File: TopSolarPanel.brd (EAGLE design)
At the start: 81 x 81 mm, 19 parts

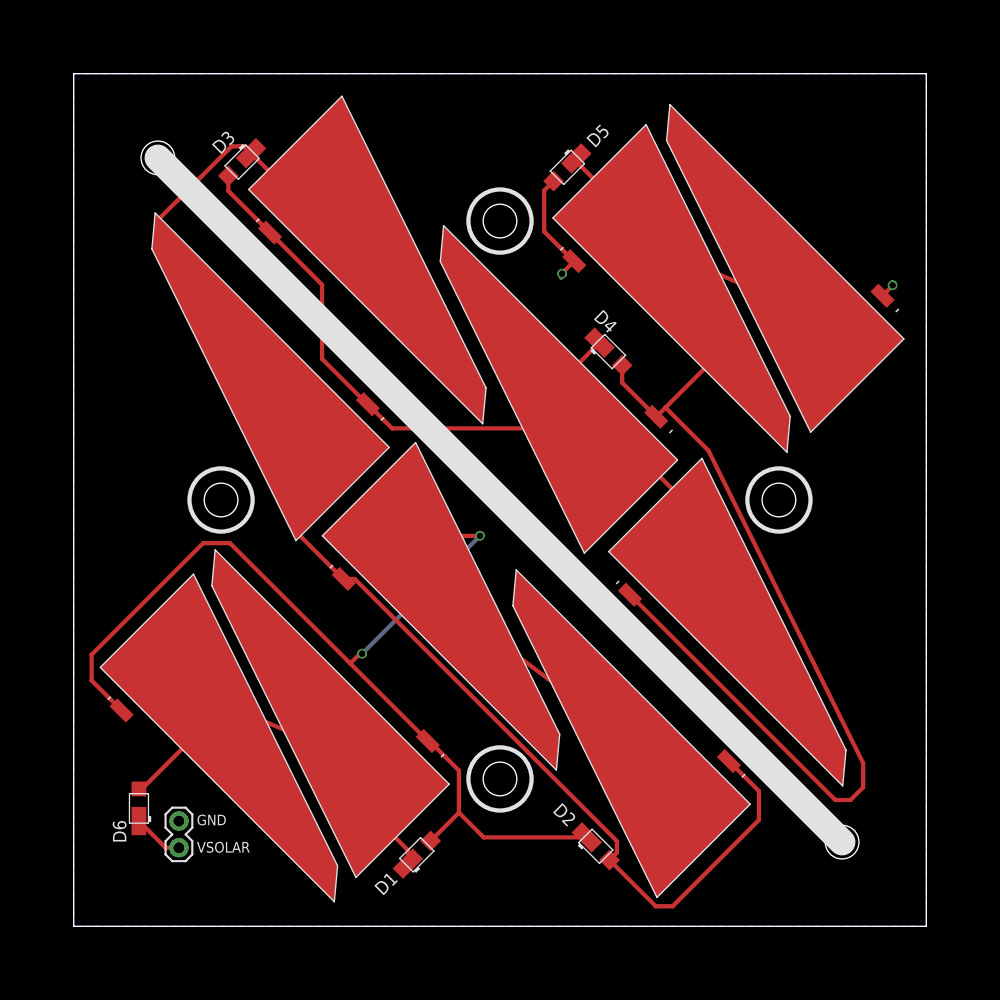
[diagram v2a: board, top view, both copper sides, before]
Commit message: Changed top board dimensions
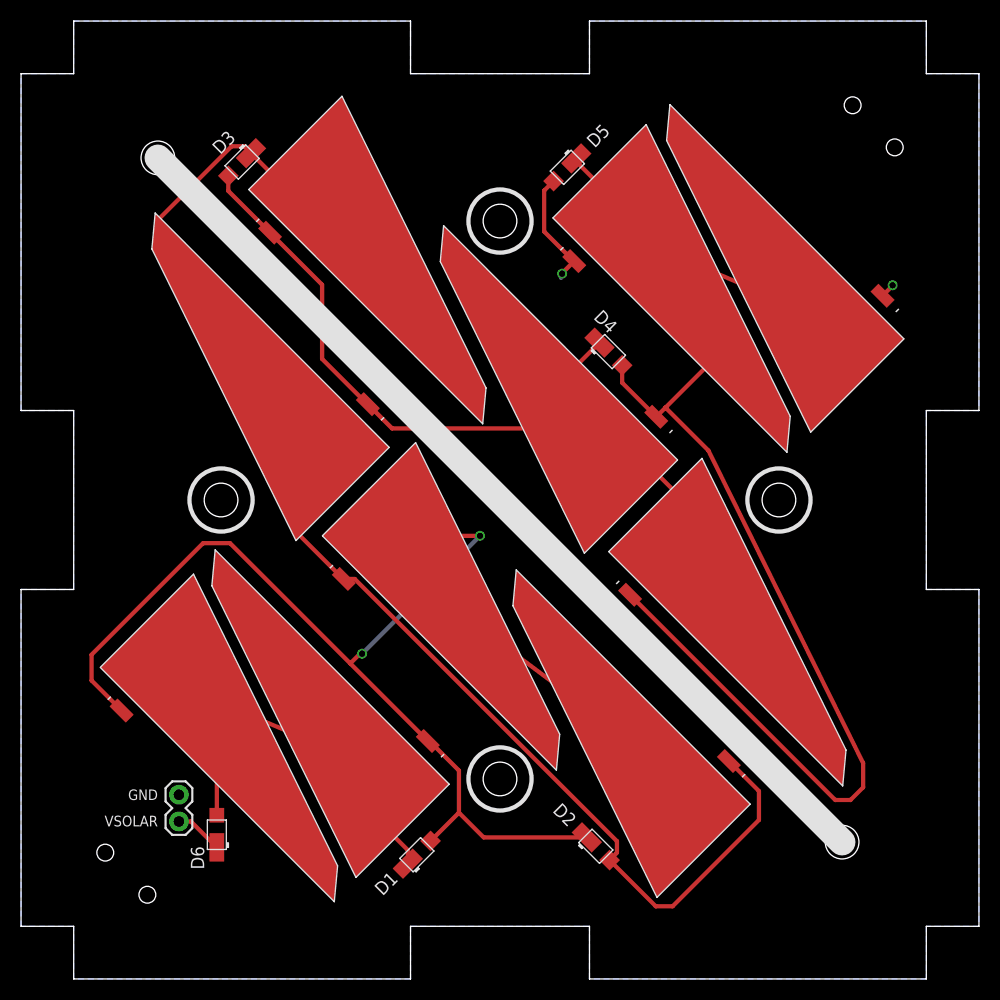
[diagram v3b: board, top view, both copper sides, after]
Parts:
- moved D6 7.81 mm to (13.6, 8.70)
- moved JP5 2.50 mm to (10.0, 12.5)
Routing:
- net N$9: track 57.5 -> 56.7 mm
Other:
- board size 81 x 81 mm -> 91 x 91 mm
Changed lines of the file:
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@@
 <board>
 <plain>
-<wire x1="0" y1="81" x2="0" y2="0" width="0" layer="20"/>
-<wire x1="0" y1="0" x2="81" y2="0" width="0" layer="20"/>
-<wire x1="81" y1="0" x2="81" y2="81" width="0" layer="20"/>
-<wire x1="81" y1="81" x2="0" y2="81" width="0" layer="20"/>
+<wire x1="0" y1="86" x2="0" y2="81" width="0" layer="20"/>
+<wire x1="0" y1="81" x2="-5" y2="81" width="0" layer="20"/>
+<wire x1="-5" y1="81" x2="-5" y2="49" width="0" layer="20"/>
+<wire x1="-5" y1="49" x2="0" y2="49" width="0" layer="20"/>
+<wire x1="0" y1="49" x2="0" y2="32" width="0" layer="20"/>
+<wire x1="0" y1="32" x2="-5" y2="32" width="0" layer="20"/>
+<wire x1="-5" y1="32" x2="-5" y2="0" width="0" layer="20"/>
+<wire x1="-5" y1="0" x2="0" y2="0" width="0" layer="20"/>
+<wire x1="0" y1="0" x2="0" y2="-5" width="0" layer="20"/>
+<wire x1="0" y1="-5" x2="32" y2="-5" width="0" layer="20"/>
+<wire x1="32" y1="-5" x2="32" y2="0" width="0" layer="20"/>
+<wire x1="32" y1="0" x2="49" y2="0" width="0" layer="20"/>
+<wire x1="49" y1="0" x2="49" y2="-5" width="0" layer="20"/>
+<wire x1="49" y1="-5" x2="81" y2="-5" width="0" layer="20"/>
+<wire x1="81" y1="-5" x2="81" y2="0" width="0" layer="20"/>
+<wire x1="81" y1="0" x2="86" y2="0" width="0" layer="20"/>
+<wire x1="86" y1="0" x2="86" y2="32" width="0" layer="20"/>
+<wire x1="86" y1="32" x2="81" y2="32" width="0" layer="20"/>
+<wire x1="81" y1="32" x2="81" y2="49" width="0" layer="20"/>
+<wire x1="81" y1="49" x2="86" y2="49" width="0" layer="20"/>
+<wire x1="86" y1="49" x2="86" y2="81" width="0" layer="20"/>
+<wire x1="86" y1="81" x2="81" y2="81" width="0" layer="20"/>
+<wire x1="81" y1="81" x2="81" y2="86" width="0" layer="20"/>
+<wire x1="81" y1="86" x2="49" y2="86" width="0" layer="20"/>
+<wire x1="49" y1="86" x2="49" y2="81" width="0" layer="20"/>
+<wire x1="49" y1="81" x2="32" y2="81" width="0" layer="20"/>
+<wire x1="32" y1="81" x2="32" y2="86" width="0" layer="20"/>
+<wire x1="32" y1="86" x2="0" y2="86" width="0" layer="20"/>
 <hole x="40.5" y="67" drill="3.2"/>
 <hole x="40.5" y="14" drill="3.2"/>
 <hole x="67" y="40.5" drill="3.2"/>
 <hole x="14" y="40.5" drill="3.2"/>
-<text x="11.7" y="9.6" size="1" layer="25" rot="SR0">GND</text>
+<text x="8" y="12.5" size="1" layer="25" rot="SR0" align="center-right">GND</text>
 <hole x="73" y="8" drill="3.2"/>
 <hole x="8" y="73" drill="3.2"/>
@@
 <circle x="40.5" y="14" radius="3" width="0.4064" layer="21"/>
 <circle x="67" y="40.5" radius="3" width="0.4064" layer="21"/>
-<text x="11.7" y="7" size="1.016" layer="21">VSOLAR</text>
+<text x="8" y="10" size="1.016" layer="21" align="center-right">VSOLAR</text>
+<hole x="3" y="7" drill="1.6"/>
+<hole x="7" y="3" drill="1.6"/>
+<hole x="74" y="78" drill="1.6"/>
+<hole x="78" y="74" drill="1.6"/>
 </plain>
 <attributes>
@@
 <attribute name="NAME" x="50.152696875" y="76.34264375" size="1.27" layer="25" rot="R225"/>
 </element>
-<element name="D6" library="Solar" package="SB_DIODE" value="SB_DIODE" x="6.2" y="11.2" rot="R90"/>
+<element name="D6" library="Solar" package="SB_DIODE" value="SB_DIODE" x="13.6" y="8.7" rot="R90"/>
 <element name="FRAME1" library="SparkFun-Aesthetics" package="CREATIVE_COMMONS" value="FRAME-LETTER" x="20" y="-13.1" smashed="yes"/>
-<element name="JP5" library="SparkFun-Connectors" package="1X02" value="M02PTH" x="10" y="10" smashed="yes" rot="R270"/>
+<element name="JP5" library="SparkFun-Connectors" package="1X02" value="M02PTH" x="10" y="12.5" smashed="yes" rot="R270"/>
 <element name="U$1" library="KickSat-Logo" package="KICKSAT_LOGO" value="KICKSAT_LOGO" x="54" y="39.3" rot="MR0"/>
 </elements>
@@
 <contactref element="SL2" pad="2"/>
 <wire x1="32.39686875" y1="13.509678125" x2="20.53076875" y2="18.45385" width="0.4064" layer="1"/>
-<wire x1="20.53076875" y1="18.45385" x2="14.43135625" y2="20.995253125" width="0.4064" layer="1"/>
+<wire x1="20.53076875" y1="18.45385" x2="14.679875" y2="20.891703125" width="0.4064" layer="1"/>
+<wire x1="14.679875" y1="20.891703125" x2="14.43135625" y2="20.995253125" width="0.4064" layer="1"/>
 <wire x1="14.43135625" y1="20.995253125" x2="5.803128125" y2="24.59031875" width="0.4064" layer="1"/>
 <wire x1="31.75146875" y1="5.95146875" x2="31.75146875" y2="7.23315" width="0.4064" layer="1"/>
 <wire x1="31.75146875" y1="7.23315" x2="20.53076875" y2="18.45385" width="0.4064" layer="1"/>
-<wire x1="6.2" y1="13.05" x2="6.486103125" y2="13.05" width="0.4064" layer="1"/>
-<wire x1="6.486103125" y1="13.05" x2="14.43135625" y2="20.995253125" width="0.4064" layer="1"/>
+<wire x1="13.6" y1="10.55" x2="13.6" y2="19.811828125" width="0.4064" layer="1"/>
+<wire x1="13.6" y1="19.811828125" x2="14.679875" y2="20.891703125" width="0.4064" layer="1"/>
 </signal>
 <signal name="VSOLAR">
 <contactref element="D6" pad="NEG"/>
 <contactref element="JP5" pad="2"/>
-<wire x1="10" y1="7.46" x2="8.74" y2="7.46" width="0.4064" layer="1"/>
-<wire x1="8.74" y1="7.46" x2="6.2" y2="10" width="0.4064" layer="1"/>
+<wire x1="10" y1="9.96" x2="11.14" y2="9.96" width="0.4064" layer="1"/>
+<wire x1="11.14" y1="9.96" x2="13.6" y2="7.5" width="0.4064" layer="1"/>
 </signal>
 <signal name="N$37">
@@
 <signal name="GND">
 <polygon width="1" layer="16" isolate="1">
+<vertex x="0" y="86"/>
+<vertex x="32" y="86"/>
+<vertex x="32" y="81"/>
+<vertex x="49" y="81"/>
+<vertex x="49" y="86"/>
+<vertex x="81" y="86"/>
+<vertex x="81" y="81"/>
+<vertex x="86" y="81"/>
+<vertex x="86" y="49"/>
+<vertex x="81" y="49"/>
+<vertex x="81" y="32"/>
+<vertex x="86" y="32"/>
+<vertex x="86" y="0"/>
+<vertex x="81" y="0"/>
+<vertex x="81" y="-5"/>
+<vertex x="49" y="-5"/>
+<vertex x="49" y="0"/>
+<vertex x="32" y="0"/>
+<vertex x="32" y="-5"/>
+<vertex x="0" y="-5"/>
+<vertex x="0" y="0"/>
+<vertex x="-5" y="0"/>
+<vertex x="-5" y="32"/>
+<vertex x="0" y="32"/>
+<vertex x="0" y="49"/>
+<vertex x="-5" y="49"/>
+<vertex x="-5" y="81"/>
 <vertex x="0" y="81"/>
-<vertex x="81" y="81"/>
-<vertex x="81" y="0"/>
-<vertex x="0" y="0"/>
 </polygon>
 <contactref element="SL9" pad="1"/>
